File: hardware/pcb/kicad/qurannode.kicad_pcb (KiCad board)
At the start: 4 copper layers, 62.8 x 150 mm, 83 parts, among them J1 USB-C-16P, J2 microSD, J3 LCD_HDR_1x14, J4 SPK_JST_PH2, J5 BATT_JST_PH2, J6 TRS_3.5, Q1 2N7002, Q2 AO3401A_PFET, Q3 2N7002_NFET, SW1 NAV_5WAY, SW2 RST, SW3 BOOT, U1 ESP32-S3-WROOM-1, U2 PCM5102A, U3 PAM8302A, U4 TP4056, U5 TPS63020, U6 USBLC6-2SC6

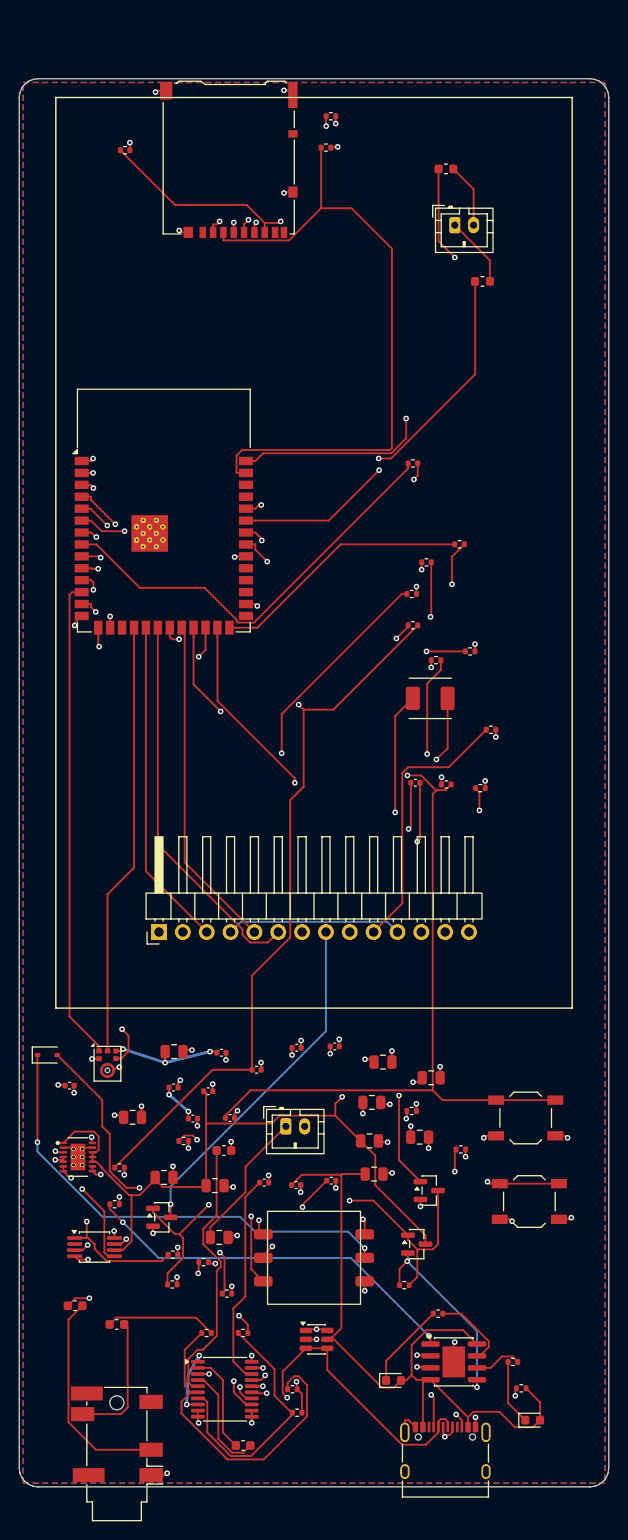
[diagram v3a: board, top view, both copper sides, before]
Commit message: Auto headphone/speaker switching: jack-detect on GPIO46 + firmware
HARDWARE (respin): wire the 3.5mm jack's tip-switch (TN) to GPIO46 so the device
senses when a plug is inserted. GPIO46 (module pin 17) is on the far side of the chip,
away from the microSD-bus corner, so it doesn't disturb SD routing (an earlier attempt
on GPIO44/pin37 broke SD_MOSI). GPIO46 is a strapping pin but is ignored in normal boot
(GPIO0 high), we flash over USB not UART, and it's only resistor-pulled (100k), so it's
safe. Added: 100k pull-up (HP_DET->3V3) + 20k tip pull-down (HP_L->GND, also DC-refs the
AC-coupled line-out). No-plug = LOW, plug = HIGH. Both existing BOM values -> no new parts.
Re-routed + re-healed to 0 unconnected / 0 electrical DRC.

FIRMWARE: Output setting is now 3-way Auto / Speaker / Headphone (default Auto).
- audio_esp32.c: read PIN_HP_DETECT (GPIO46, floating input); use_speaker() = forced
  speaker/headphone, or in Auto route to line-out (amp off) when a plug is present.
  Added hal_audio_headphone_present().
- hal.h: set_output(mode) 0/1/2; new headphone_present() query.
- prefs.c: default output=2 (auto), clamp <=2. scene_settings.c: cycle 3 modes; the
  Output row shows "Auto (Speaker)" / "Auto (Headphone)" live.
- audio_sim.cpp: headphone_present() stub returns 0 (no jack in sim). Sim builds clean.

Co-Authored-By: Claude Opus 4.8 (1M context) <noreply@anthropic.com>
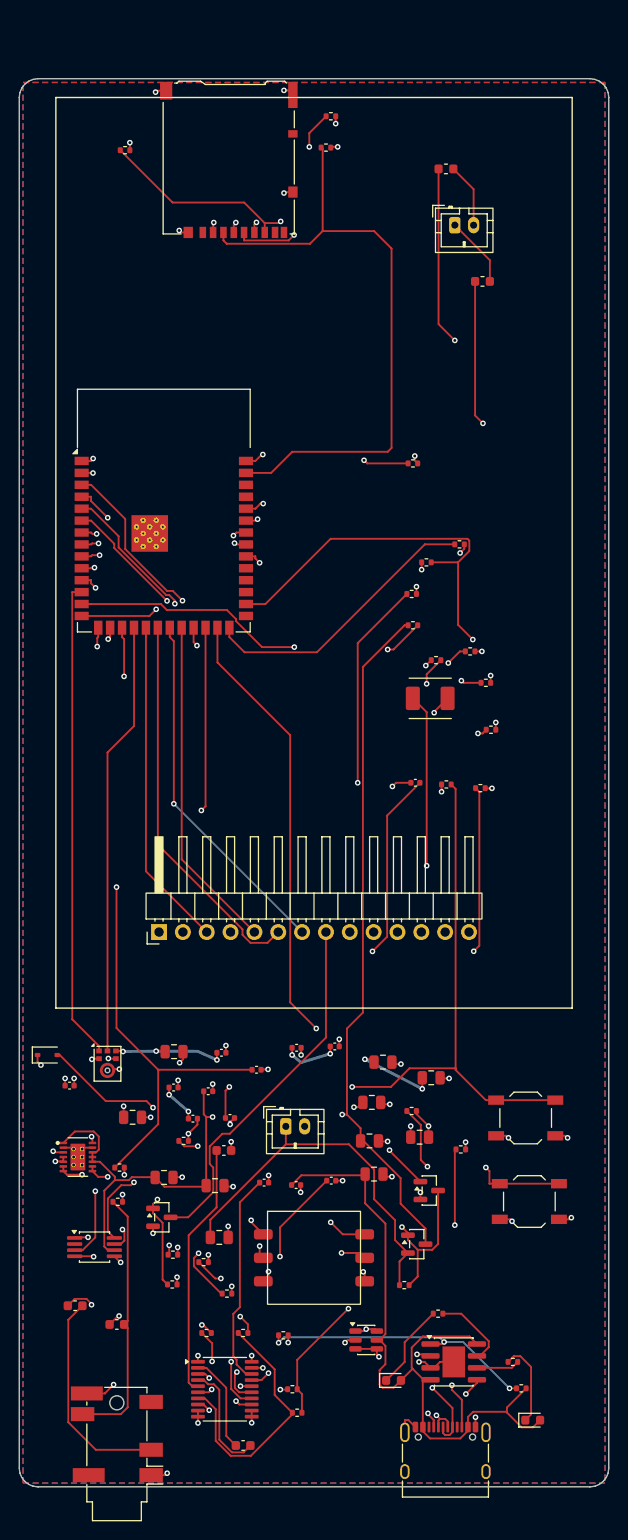
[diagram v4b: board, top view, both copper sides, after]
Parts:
- added R31: 10k, R_0402_1005Metric, F.Cu at (32.7, 7.34)
- added R32: 10k, R_0402_1005Metric, F.Cu at (11.3, 7.62)
- R21: value 20k -> 100k
- R23: value 100k -> 20k
- R24: value 4k7 -> 20k
- R25: value 4k7 -> 100k
- R26: value 100R -> 4k7
- R27: value 10k -> 4k7
- R28: value 10k -> 100R
- moved R29 122.2 mm to (16.3, 128.4)
- moved R24 83.2 mm to (29.6, 142.1)
- moved R21 78.0 mm to (49.7, 64.4)
- moved R27 68.2 mm to (50.3, 69.3)
- moved R25 65.4 mm to (16.4, 125.3)
- moved R28 38.0 mm to (41.9, 41.0)
- moved R22 29.5 mm to (10.5, 119.6)
- moved R5 22.8 mm to (28.1, 133.9)
- moved R30 22.2 mm to (33.2, 4.00)
- moved R26 20.9 mm to (48.0, 61.0)
- moved R23 19.2 mm to (29.1, 139.6)
- moved U6 5.28 mm to (37.0, 134.4)
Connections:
- J6 pad TN: (no net) -> HP_DET
- R21 pad 1: OUTL -> HP_DET
- R21 pad 2: AIN -> +3V3
- R22 pad 1: OUTR -> HP_L
- R22 pad 2: AIN -> GND
- R23 pad 1: AMP_EN -> OUTL
- R23 pad 2: GND -> AIN
- R24 pad 1: TOUCH_SDA -> OUTR
- R24 pad 2: +3V3 -> AIN
- R25 pad 1: TOUCH_SCL -> AMP_EN
- R25 pad 2: +3V3 -> GND
- R26 pad 1: DISP_BL -> TOUCH_SDA
- R26 pad 2: BL_G -> +3V3
- R27 pad 1: BL_G -> TOUCH_SCL
- R27 pad 2: GND -> +3V3
- R28 pad 1: SD_CS -> DISP_BL
- R28 pad 2: +3V3 -> BL_G
- R29 pad 1: SD_MOSI -> BL_G
- R29 pad 2: +3V3 -> GND
- R30 pad 1: SD_MISO -> SD_CS
- U1 pad 17: (no net) -> HP_DET
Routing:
- net HP_DET: track 0.00 -> 122.8 mm, vias 0 -> 3
- net VBAT: track 56.0 -> 81.9 mm, vias 2 -> 1
- net N$4: track 53.7 -> 30.2 mm
- net OUTL: track 34.8 -> 16.4 mm, vias 0 -> 3
- net TOUCH_SCL: track 97.4 -> 82.4 mm, vias 1 -> 2
- net EN: track 127.6 -> 142.6 mm, vias 2 -> 3
- net HP_L: track 14.1 -> 28.0 mm
- net N$21: track 149.2 -> 136.4 mm
- net IO0: track 96.6 -> 107.4 mm, vias 3 -> 2
- net USB_DP: track 124.5 -> 133.5 mm
- net N$7: track 67.4 -> 75.8 mm
- net NAV_MID: track 112.7 -> 104.5 mm
- net +3V3: track 44.2 -> 51.5 mm, vias 29 -> 30
- net DISP_BL: track 45.6 -> 38.6 mm, vias 0 -> 2
- net USB_DM: track 127.8 -> 121.3 mm, vias 2 -> 3
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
